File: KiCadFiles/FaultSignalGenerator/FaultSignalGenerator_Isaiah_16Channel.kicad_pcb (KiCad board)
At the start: 2 copper layers, 280 parts, among them J1 Conn_02x20_Odd_Even, J2 Conn_02x16_Odd_Even, J3 DB25_Receptacle, U1 MCP4431-503E/ST, U10 TL074CDR, U11 TL074CDR, U12 TL074CDR, U13 TL074CDR, U14 PCM1681PWP, U15 PCM1681PWP, U16 TL780-05CKTTR, U2 MCP4431-503E/ST, U3 MCP4431-503E/ST, U4 MCP4431-503E/ST, U5 TL074CDR, U6 TL074CDR, U7 TL074CDR, U8 TL074CDR, U9 TL074CDR

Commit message: update pcb
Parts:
- C57, C70, C71, C72, C76, C77, C78, R120, R121, R122, R138, R139: moved to B.Cu
- moved C72 158.5 mm to (210.8, 64.5)
- moved C78 155.8 mm to (210.8, 59.4)
- moved C57 152.9 mm to (240.1, 138.7), turned to 180 degrees
- moved C71 151.8 mm to (208.3, 68.1), turned to 180 degrees
- moved C70 147.6 mm to (214.3, 76.7), turned to 180 degrees
- moved R139 146.6 mm to (212.1, 55.8), turned to -90 degrees
- moved C77 141.7 mm to (208.8, 73.4), turned to 180 degrees
- moved C76 137.3 mm to (214.0, 81.8), turned to 180 degrees
- moved R136 127.2 mm to (205.4, 59.3), turned to 0 degrees
- moved C73 127.2 mm to (219.0, 79.2)
- moved R138 125.1 mm to (206.8, 77.4), turned to 90 degrees
- moved R131 122.1 mm to (214.3, 79.2), turned to 0 degrees
- moved R135 120.9 mm to (213.9, 73.4)
- moved R137 116.2 mm to (212.4, 85.6), turned to 90 degrees
- moved R120 115.5 mm to (212.2, 116.8), turned to 90 degrees
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
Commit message: PCB layout from basic Pi-DAC connection to start of filtering
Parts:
- C48, C49, C50, C51, C52, C53: moved to B.Cu
- moved R53 188.0 mm to (231.2, 73.4), turned to 180 degrees
- moved R52 185.4 mm to (231.2, 76.2), turned to 180 degrees
- moved R51 182.9 mm to (231.1, 79.1), turned to 180 degrees
- moved R50 180.7 mm to (231.1, 81.8), turned to 180 degrees
- moved R49 178.7 mm to (231.1, 84.4), turned to 180 degrees
- moved R76 175.9 mm to (231.5, 64.6), turned to 180 degrees
- moved R75 172.7 mm to (231.3, 67.6), turned to 180 degrees
- moved R74 169.7 mm to (231.1, 70.6), turned to 180 degrees
- moved C35 161.3 mm to (241.9, 67.7), turned to 180 degrees
- moved C33 160.5 mm to (241.6, 79.1), turned to 180 degrees
- moved C34 160.5 mm to (241.8, 73.4), turned to 180 degrees
- moved C31 159.3 mm to (258.9, 114.4)
- moved C30 155.9 mm to (252.4, 121.9)
- moved C43 155.7 mm to (241.9, 64.6), turned to 180 degrees
- moved R93 154.0 mm to (258.6, 117.0), turned to 180 degrees
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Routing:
- net SDA: track 0.00 -> 1.96 mm
- net SCL: track 0.00 -> 1.34 mm
- net Net-(U15-SCK): track 0.00 -> 0.87 mm
- net Net-(U15-VOUT2): track 0.00 -> 0.80 mm
- net Net-(U15-DATA1): track 0.00 -> 0.65 mm
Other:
- board text added: "DAC Connection"
- board text added: "Gain Stage"
- board text added: "LED Bank"
- board text added: "Pi Connection"
- board text added: "Power Block"

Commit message: update filter block
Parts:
- C1, C10, C11, C12, C13, C14, C15, C17, C18, C19, C2, C20, C21, C22, C23, C24, C25, C26, C3, C30, C4, C5, C6, C7, C8, C9, R54, R55, R56, R57, R58, R59, R60, R61, R62, R63, R64, R65, R66, R67, R68, R69, R70, R71, R72, R73, R77, R78, R79, R80, R81, R82, R83, R84, R85, R86, R87, R88, R89, R90, R91, R92, R93, R95, R96, R97, R98, R99, U4: moved to B.Cu
- U13: moved to F.Cu
- moved U13 243.1 mm to (247.2, 89.5)
- moved C28 228.6 mm to (251.3, 82.1), turned to 90 degrees
- moved C26 219.1 mm to (244.6, 86.5)
- moved R89 217.0 mm to (244.8, 82.3), turned to -90 degrees
- moved C29 216.8 mm to (247.4, 81.5), turned to 90 degrees
- moved R90 216.3 mm to (242.4, 82.3), turned to 90 degrees
- moved R91 213.8 mm to (240.7, 87.7), turned to 90 degrees
- moved C14 213.6 mm to (235.0, 55.2)
- moved U5 210.2 mm to (227.2, 68.2), turned to 90 degrees
- moved C4 209.6 mm to (235.1, 60.1)
- moved C6 205.4 mm to (237.6, 78.4), turned to 180 degrees
- moved C27 202.2 mm to (236.0, 86.2)
- moved U6 199.8 mm to (201.1, 58.6), turned to 90 degrees
- moved R72 198.8 mm to (236.3, 51.5), turned to -90 degrees
- moved C9 197.9 mm to (229.9, 57.7)
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
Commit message: finish layout
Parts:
- C100, C16, C31, C85, C86, C87, C88, C89, C90, C91, C92, C93, C94, C95, C96, C97, C98, C99, R143, R144, R145, R146, R147, R148, R149, R150, R151, R152, R153, R154, R155, R156, R157, R158, R94: moved to B.Cu
- C48, C49: footprint Capacitor_SMD:CP_Elec_4x5.4 -> Capacitor_SMD:C_1206_3216Metric_Pad1.33x1.80mm_HandSolder
- R23, R47, U4: moved to F.Cu
- moved C16 197.4 mm to (254.5, 91.3), turned to 180 degrees
- moved U10 173.4 mm to (211.3, 65.6), turned to 90 degrees
- moved U3 167.9 mm to (220.1, 65.6), turned to -90 degrees
- moved U11 166.6 mm to (210.7, 114.3), turned to 90 degrees
- moved R33 164.2 mm to (223.8, 58.6), turned to -90 degrees
- moved R34 163.7 mm to (221.6, 58.6), turned to -90 degrees
- moved U2 156.6 mm to (220.2, 114.6), turned to -90 degrees
- moved R21 153.8 mm to (224.0, 106.9), turned to -90 degrees
- moved R41 152.0 mm to (223.8, 72.9), turned to -90 degrees
- moved R22 151.8 mm to (221.6, 106.9), turned to -90 degrees
- moved R42 151.1 mm to (221.4, 72.9), turned to -90 degrees
- moved R43 150.3 mm to (219.2, 72.8), turned to -90 degrees
- moved R24 148.1 mm to (217.0, 106.9), turned to -90 degrees
- moved R29 147.8 mm to (224.2, 122.1), turned to -90 degrees
- moved R35 145.9 mm to (219.3, 58.6), turned to -90 degrees
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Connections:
- J3 pad 1: /Amplification Stage/out1 -> /Amplification Stage/out13
- J3 pad 10: /Amplification Stage/out10 -> /Amplification Stage/out4
- J3 pad 11: /Amplification Stage/out11 -> /Amplification Stage/out3
- J3 pad 12: /Amplification Stage/out12 -> /Amplification Stage/out2
- J3 pad 13: /Amplification Stage/out13 -> /Amplification Stage/out1
- J3 pad 14: /Amplification Stage/out14 -> unconnected-(J3-P14-Pad14)
- J3 pad 15: /Amplification Stage/out15 -> unconnected-(J3-P15-Pad15)
- J3 pad 16: /Amplification Stage/out16 -> unconnected-(J3-P16-Pad16)
- J3 pad 2: /Amplification Stage/out2 -> /Amplification Stage/out12
- J3 pad 23: unconnected-(J3-P23-Pad23) -> /Amplification Stage/out16
- J3 pad 24: unconnected-(J3-P24-Pad24) -> /Amplification Stage/out15
- J3 pad 25: unconnected-(J3-P25-Pad25) -> /Amplification Stage/out14
- J3 pad 3: /Amplification Stage/out3 -> /Amplification Stage/out11
- J3 pad 4: /Amplification Stage/out4 -> /Amplification Stage/out10
- J3 pad 5: /Amplification Stage/out5 -> /Amplification Stage/out9
- J3 pad 6: /Amplification Stage/out6 -> /Amplification Stage/out8
- J3 pad 8: /Amplification Stage/out8 -> /Amplification Stage/out6
- J3 pad 9: /Amplification Stage/out9 -> /Amplification Stage/out5
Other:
- board text removed: "Gain Stage"
- board text removed: "LED Bank"

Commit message: start routing
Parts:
- turned R92 to 180 degrees
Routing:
- net Net-(U14-SCK): track 0.00 -> 6.97 mm, vias 0 -> 1
- net +3.3V: track 0.00 -> 5.30 mm, vias 0 -> 1
- net Net-(U14-DATA1): track 0.00 -> 4.07 mm, vias 0 -> 1
- net Net-(U14-LRCK): track 0.00 -> 3.62 mm, vias 0 -> 1
- net Net-(U14-BCK): track 0.00 -> 3.36 mm, vias 0 -> 1
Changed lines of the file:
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@@
   )
   (footprint "Resistor_SMD:R_1206_3216Metric" (layer "B.Cu")
-    (at 260.9375 73.3)
+    (at 260.9375 73.3 180)
     (descr "Resistor SMD 1206 (3216 Metric), square (rectangular) end terminal, IPC_7351 nominal, (Body size source: IPC-SM-782 page 72, https://www.pcb-3d.com/wordpress/wp-content/uploads/ipc-sm-782a_amendment_1_and_2.pdf), generated with kicad-footprint-generator")
     (tags "resistor")
@@
     (property "ki_keywords" "R res resistor")
     (attr smd)
-    (fp_text reference "R92" (at 3.6625 0.1) (layer "B.SilkS")
+    (fp_text reference "R92" (at -3.6125 -0.1) (layer "B.SilkS")
         (effects (font (size 1 1) (thickness 0.15)) (justify mirror))
     )
@@
     (fp_line (start 1.6 0.8) (end 1.6 -0.8)
       (stroke (width 0.1) (type solid)) (layer "B.Fab"))
-    (pad "1" smd roundrect (at -1.4625 0) (size 1.125 1.75) (layers "B.Cu" "B.Paste" "B.Mask") (roundrect_rratio 0.222222)
+    (pad "1" smd roundrect (at -1.4625 0 180) (size 1.125 1.75) (layers "B.Cu" "B.Paste" "B.Mask") (roundrect_rratio 0.222222)
       (net 172 "TDMA_SCK") (pintype "passive"))
-    (pad "2" smd roundrect (at 1.4625 0) (size 1.125 1.75) (layers "B.Cu" "B.Paste" "B.Mask") (roundrect_rratio 0.222222)
+    (pad "2" smd roundrect (at 1.4625 0 180) (size 1.125 1.75) (layers "B.Cu" "B.Paste" "B.Mask") (roundrect_rratio 0.222222)
       (net 173 "Net-(U14-SCK)") (pintype "passive"))
     (model "${KICAD6_3DMODEL_DIR}/Resistor_SMD.3dshapes/R_1206_3216Metric.wrl"
@@
     (effects (font (size 1.5 1.5) (thickness 0.3) bold) (justify left bottom))
   )
+  (segment (start 258.954188 68.079188) (end 259.475 68.6) (width 0.2) (layer "F.Cu") (net 157))
+  (segment (start 256.326887 68.079188) (end 258.954188 68.079188) (width 0.2) (layer "F.Cu") (net 157))
+  (via (at 259.475 68.6) (size 0.6) (drill 0.3) (layers "F.Cu" "B.Cu") (net 157))
   (segment (start 257.138685 108.236078) (end 256.4855 108.236078) (width 0.2) (layer "F.Cu") (net 159))
+  (segment (start 257.254188 68.729188) (end 259.475 70.95) (width 0.2) (layer "F.Cu") (net 165))
+  (segment (start 256.326887 68.729188) (end 257.254188 68.729188) (width 0.2) (layer "F.Cu") (net 165))
+  (via (at 259.475 70.95) (size 0.6) (drill 0.3) (layers "F.Cu" "B.Cu") (net 165))
   (segment (start 256.3355 109.036078) (end 256.4855 108.886078) (width 0.2) (layer "F.Cu") (net 169))
   (segment (start 256.988685 109.036078) (end 256.3355 109.036078) (width 0.2) (layer "F.Cu") (net 169))
+  (segment (start 256.326887 67.429188) (end 257.420812 67.429188) (width 0.2) (layer "F.Cu") (net 171))
+  (segment (start 259.375 66.4) (end 259.475 66.3) (width 0.2) (layer "F.Cu") (net 171))
+  (segment (start 258.45 66.4) (end 259.375 66.4) (width 0.2) (layer "F.Cu") (net 171))
+  (segment (start 257.420812 67.429188) (end 258.45 66.4) (width 0.2) (layer "F.Cu") (net 171))
+  (via (at 259.475 66.3) (size 0.6) (drill 0.3) (layers "F.Cu" "B.Cu") (net 171))
+  (segment (start 259.225 73.55) (end 259.475 73.3) (width 0.2) (layer "F.Cu") (net 173))
+  (segment (start 256.980072 69.379188) (end 257.75 70.149116) (width 0.2) (layer "F.Cu") (net 173))
+  (segment (start 257.75 73.55) (end 259.225 73.55) (width 0.2) (layer "F.Cu") (net 173))
+  (segment (start 256.326887 69.379188) (end 256.980072 69.379188) (width 0.2) (layer "F.Cu") (net 173))
+  (segment (start 257.75 70.149116) (end 257.75 73.55) (width 0.2) (layer "F.Cu") (net 173))
+  (via (at 259.475 73.3) (size 0.6) (drill 0.3) (layers "F.Cu" "B.Cu") (net 173))
   (segment (start 256.980072 70.679188) (end 256.326887 70.679188) (width 0.2) (layer "F.Cu") (net 205))
   (segment (start 257.153502 110.186078) (end 256.4855 110.186078) (width 0.2) (layer "F.Cu") (net 205))
@@
   (segment (start 256.326887 70.029188) (end 255.673702 70.029188) (width 0.2) (layer "F.Cu") (net 206))
   (segment (start 255.832315 109.536078) (end 256.4855 109.536078) (width 0.2) (layer "F.Cu") (net 206))
+  (segment (start 257.9 64.2) (end 259.2375 64.2) (width 0.2) (layer "F.Cu") (net 238))
+  (segment (start 256.326887 66.779188) (end 256.980072 66.779188) (width 0.2) (layer "F.Cu") (net 238))
+  (segment (start 256.980072 66.779188) (end 257.9 65.85926) (width 0.2) (layer "F.Cu") (net 238))
+  (segment (start 257.9 65.85926) (end 257.9 64.2) (width 0.2) (layer "F.Cu") (net 238))
+  (segment (start 259.2375 64.2) (end 259.4875 63.95) (width 0.2) (layer "F.Cu") (net 238))
+  (via (at 259.4875 63.95) (size 0.6) (drill 0.3) (layers "F.Cu" "B.Cu") (net 238))
   (segment (start 250.7605 110.186078) (end 249.963517 110.186078) (width 0.2) (layer "F.Cu") (net 248))
 )

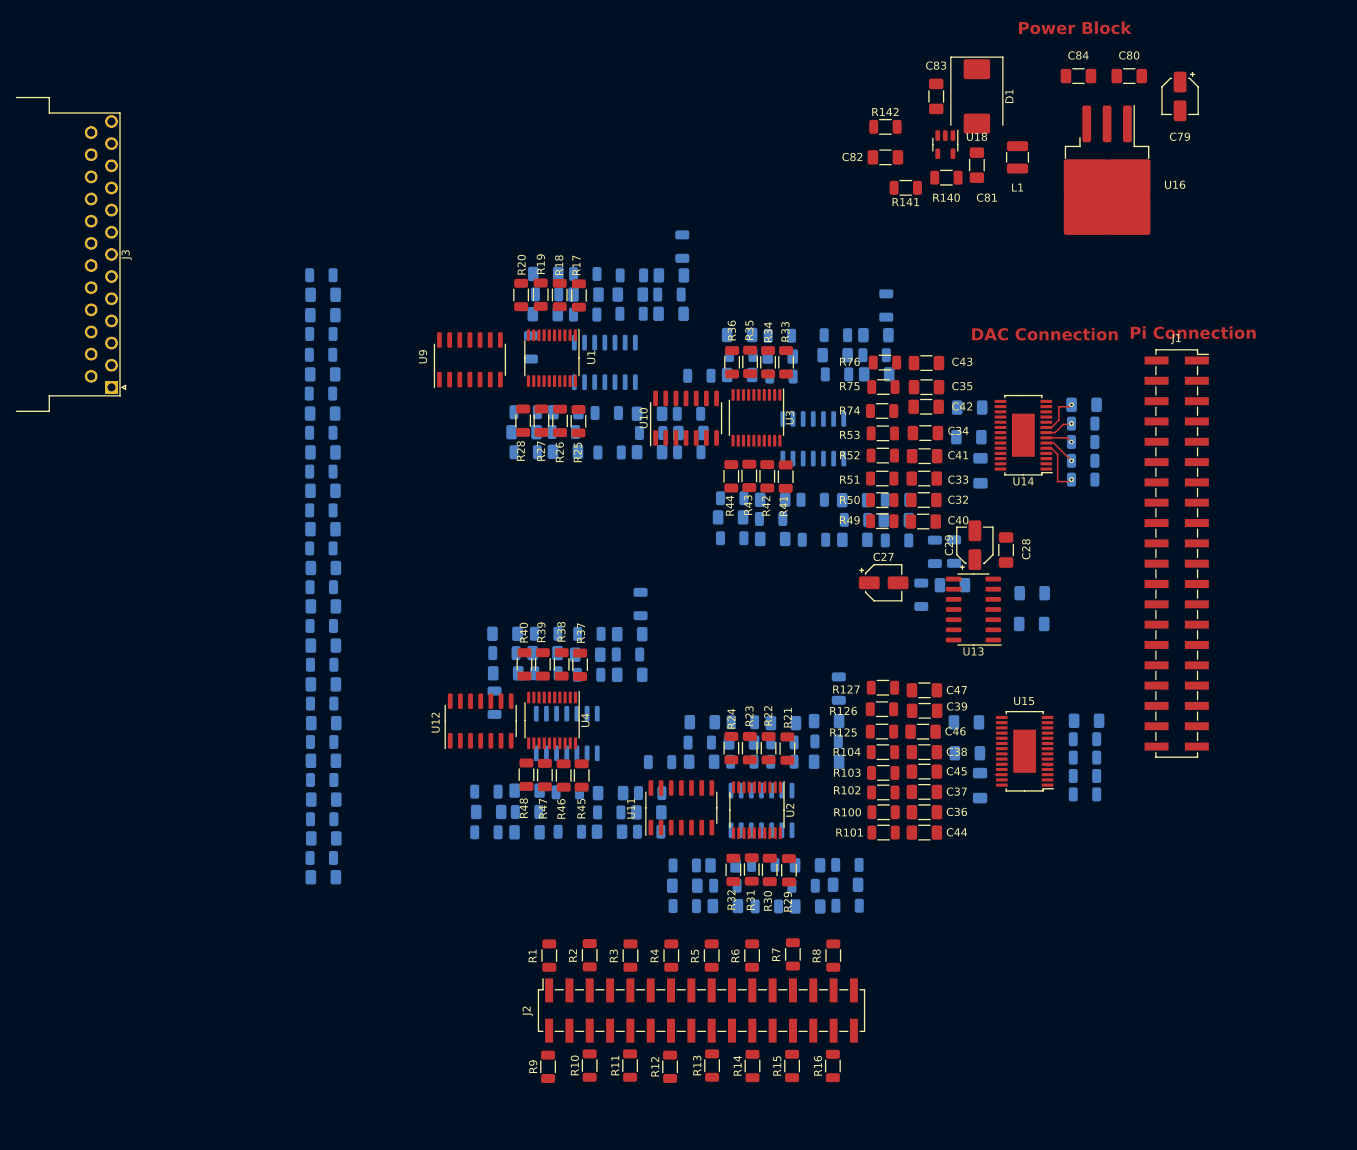
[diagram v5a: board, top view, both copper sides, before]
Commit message: Routing work
Basic top and bottom routing. Haven't interconnected them, or hooked up the power layer to connect all the 5V, 12V, 3.3V, and 0V potential pins together
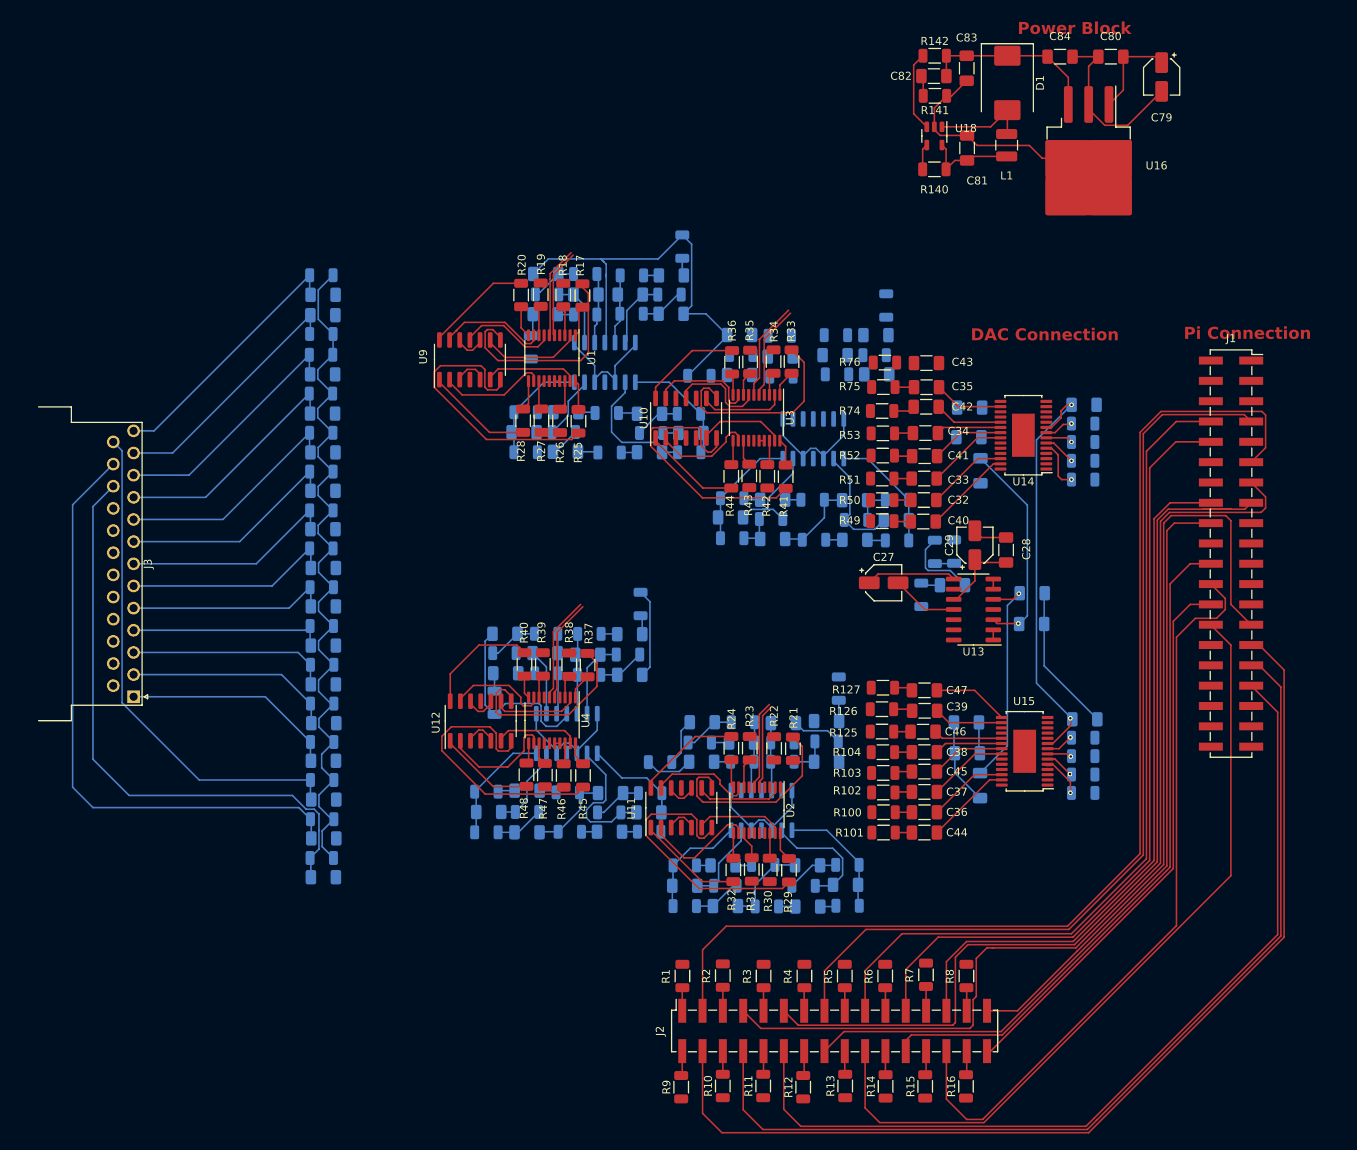
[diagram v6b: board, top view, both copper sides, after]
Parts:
- moved J3 38.8 mm to (142.2, 100.4)
- moved J2 16.8 mm to (229.9, 142.2)
- moved R14 16.8 mm to (236.2, 149.2)
- moved R1 16.8 mm to (210.8, 135.3)
- moved R3 16.8 mm to (221.0, 135.3)
- moved R4 16.8 mm to (226.1, 135.3)
- moved R8 16.8 mm to (246.3, 135.3)
- moved R12 16.8 mm to (225.9, 149.2)
- moved R15 16.8 mm to (241.2, 149.2)
- moved R16 16.8 mm to (246.3, 149.2)
- moved R2 16.8 mm to (215.9, 135.3)
- moved R9 16.8 mm to (210.7, 149.2)
- moved R10 16.8 mm to (215.9, 149.1)
- moved R11 16.8 mm to (220.9, 149.1)
- moved R13 16.8 mm to (231.2, 149.1)
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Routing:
- net 0: track 0.00 -> 356.6 mm
- net LED1: track 0.00 -> 143.5 mm
- net LED9: track 0.00 -> 130.4 mm
- net LED2: track 0.00 -> 126.9 mm
- net LED10: track 0.00 -> 121.5 mm
- net LED3: track 0.00 -> 119.5 mm
- net LED4: track 0.00 -> 118.3 mm
- net LED11: track 0.00 -> 112.3 mm
- net LED5: track 0.00 -> 106.5 mm
- net LED12: track 0.00 -> 100.2 mm
- net LED6: track 0.00 -> 99.4 mm
- net LED13: track 0.00 -> 98.8 mm
- net LED8: track 0.00 -> 95.4 mm
- net LED15: track 0.00 -> 93.4 mm
- net LED7: track 0.00 -> 88.0 mm
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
